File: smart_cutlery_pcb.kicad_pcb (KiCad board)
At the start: 2 copper layers, 55 parts, among them J1 CONN_01X05, J2 CONN_01X04, Q1 Q_PMOS_DGS, Q2 BC849, Q3 BC849, SW1 SW_Push, SW2 SW_Push, U1 STM32L053C6Tx, U2 MODULE-BLUETOOTH-HC-05(34P-27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, U3 NCP1402SN33T1G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

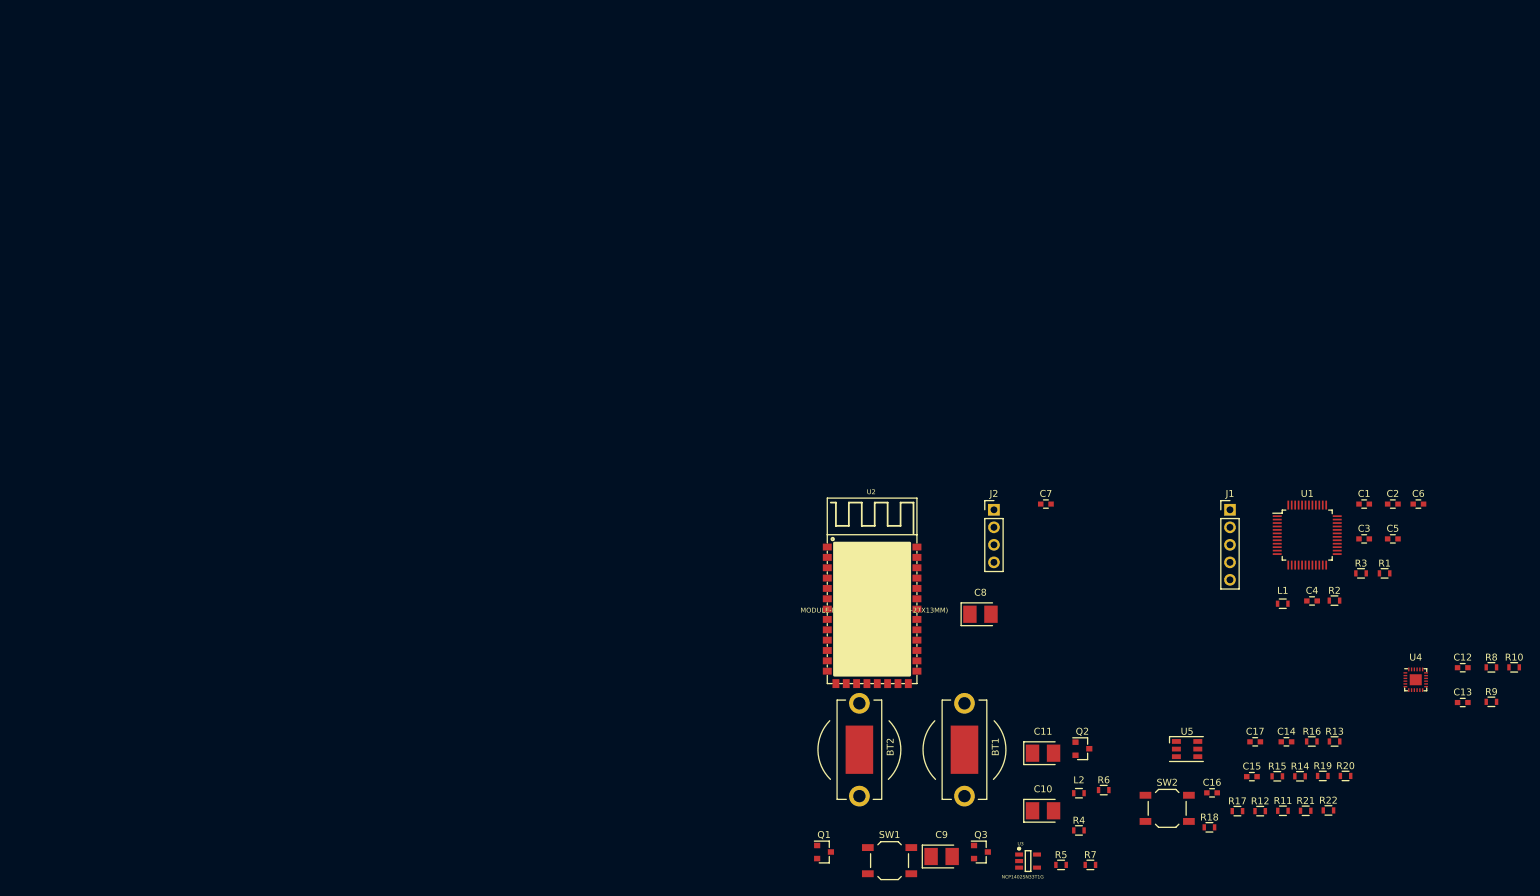
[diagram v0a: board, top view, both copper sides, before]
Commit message: Update to new soft-latching power circuit
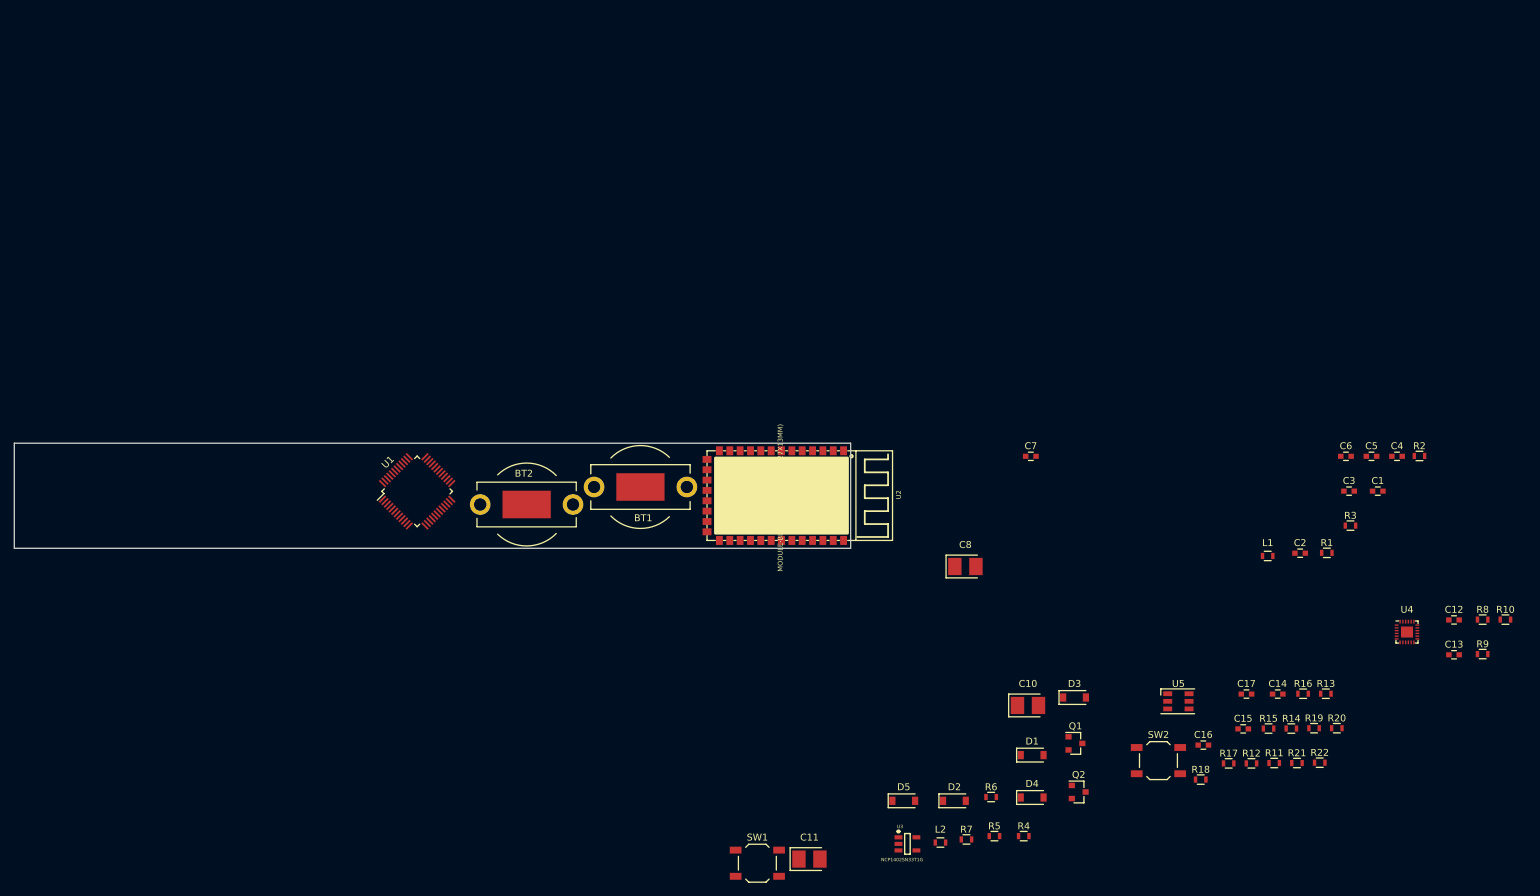
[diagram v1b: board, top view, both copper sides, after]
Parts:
- removed C9: 22uF, Capacitors_Tantalum_SMD:CP_Tantalum_Case-B_EIA-3528-21_Reflow
- removed Q3: BC849, TO_SOT_Packages_SMD:SOT-23
- added D1: MBR0520, Diodes_SMD:D_SOD-123, F.Cu at (210.5, 140.5)
- added D2: MBR0520, Diodes_SMD:D_SOD-123, F.Cu at (199.2, 147.1)
- added D3: MBR0520, Diodes_SMD:D_SOD-123, F.Cu at (216.6, 132.1)
- added D4: MBR0520, Diodes_SMD:D_SOD-123, F.Cu at (210.5, 146.6)
- added D5: MBR0520, Diodes_SMD:D_SOD-123, F.Cu at (191.9, 147.1)
- Q1: value Q_PMOS_DGS -> BSS84
- Q2: value BC849 -> BSS138
- R6: value 1M -> 4K7
- R7: value 100K -> 47K
- SW1, SW2: value SW_Push -> TL3342
- moved U1 129.2 mm to (121.3, 102.2), turned to 45 degrees
- moved BT1 60.5 mm to (153.7, 101.6), turned to 0 degrees
- moved J1 60.2 mm to (179.1, 101.0), turned to 270 degrees
- moved BT2 59.9 mm to (137.2, 104.1), turned to 180 degrees
- moved Q1 39.7 mm to (216.7, 138.8)
- moved C11 37.2 mm to (178.2, 155.6)
- moved U2 36.3 mm to (163.3, 102.8), turned to 270 degrees
- moved J2 34.8 mm to (170.2, 106.0), turned to 90 degrees
- moved R2 24.3 mm to (266.6, 97.1)
- moved C4 24.3 mm to (263.4, 97.2)
- moved L2 21.3 mm to (197.2, 153.2)
- moved SW1 19.2 mm to (170.6, 156.2)
- moved R7 18.3 mm to (200.9, 152.7)
- moved U3 17.7 mm to (192.4, 153.4)
- moved R6 16.4 mm to (204.5, 146.6)
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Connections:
- net /mode_switch renamed /MODE_BTN
- Q1 pad 1: Net-(C10-Pad1) -> Net-(Q1-Pad1)
- Q1 pad 2: Net-(Q1-Pad2) -> Net-(D1-Pad1)
- Q1 pad 3: Net-(D1-Pad1) -> Net-(C10-Pad1)
- Q2 pad 1: Net-(Q2-Pad1) -> /PWR_LATCH
- Q2 pad 3: Net-(Q1-Pad2) -> Net-(Q1-Pad1)
- R11 pad 1: /touch_interface/sense_y1 -> (no net)
- R12 pad 1: /touch_interface/sense_y2 -> (no net)
- R13 pad 1: /touch_interface/sense_y3 -> (no net)
- R14 pad 1: /touch_interface/sense_y4 -> (no net)
- R15 pad 1: /touch_interface/sense_x1 -> (no net)
- R16 pad 1: /touch_interface/sense_x2 -> (no net)
- R17 pad 1: /touch_interface/sense_x3 -> (no net)
- R18 pad 1: /touch_interface/sense_x4 -> (no net)
- R4 pad 1: Net-(D1-Pad1) -> Net-(Q1-Pad1)
- R4 pad 2: Net-(Q1-Pad2) -> Net-(D1-Pad1)
- R5 pad 1: Net-(C10-Pad1) -> GND
- R5 pad 2: Net-(Q2-Pad1) -> /PWR_LATCH
- R6 pad 1: Net-(C10-Pad1) -> /PWR_BUTTON
- R7 pad 1: Net-(D1-Pad1) -> GND
- R7 pad 2: Net-(Q3-Pad3) -> /PWR_BUTTON
- SW1 pad 1: Net-(Q2-Pad1) -> Net-(D1-Pad1)
- SW1 pad 2: Net-(Q3-Pad3) -> Net-(D4-Pad2)
- U1 pad 2: Net-(U1-Pad2) -> (no net)
- U1 pad 20: /micro/PB2 -> (no net)
- U1 pad 25: /micro/PB12 -> (no net)
- U1 pad 27: /micro/PB14 -> /PWR_BUTTON
- U1 pad 28: /micro/PB15 -> /PWR_LATCH
- U1 pad 29: /micro/PA8 -> (no net)
- U1 pad 3: Net-(U1-Pad3) -> (no net)
- U1 pad 33: /micro/PA12 -> (no net)
- U1 pad 38: /micro/PA15 -> (no net)
- U1 pad 4: Net-(U1-Pad4) -> (no net)
- U1 pad 40: /micro/PB4 -> (no net)
- U1 pad 41: /micro/PB5 -> (no net)
- U1 pad 5: Net-(U1-Pad5) -> (no net)
- U1 pad 6: Net-(U1-Pad6) -> (no net)
- U2 pad 10: Net-(U2-Pad10) -> (no net)
- U2 pad 11: Net-(U2-Pad11) -> (no net)
- U2 pad 14: Net-(U2-Pad14) -> (no net)
- U2 pad 15: Net-(U2-Pad15) -> (no net)
- U2 pad 20: Net-(U2-Pad20) -> (no net)
- U2 pad 21: Net-(U2-Pad21) -> (no net)
- U2 pad 22: Net-(U2-Pad22) -> (no net)
- U2 pad 23: Net-(U2-Pad23) -> (no net)
- U2 pad 24: Net-(U2-Pad24) -> (no net)
- U2 pad 25: Net-(U2-Pad25) -> (no net)
- U2 pad 26: Net-(U2-Pad26) -> (no net)
- U2 pad 27: Net-(U2-Pad27) -> (no net)
- U2 pad 28: Net-(U2-Pad28) -> (no net)
- U2 pad 29: Net-(U2-Pad29) -> (no net)
- U2 pad 3: Net-(U2-Pad3) -> (no net)
- U2 pad 30: Net-(U2-Pad30) -> (no net)
- U2 pad 31: Net-(U2-Pad31) -> (no net)
- U2 pad 32: Net-(U2-Pad32) -> (no net)
- U2 pad 33: Net-(U2-Pad33) -> (no net)
- U2 pad 34: Net-(U2-Pad34) -> (no net)
- U2 pad 4: Net-(U2-Pad4) -> (no net)
- U2 pad 5: Net-(U2-Pad5) -> (no net)
- U2 pad 6: Net-(U2-Pad6) -> (no net)
- U2 pad 7: Net-(U2-Pad7) -> (no net)
- U2 pad 8: Net-(U2-Pad8) -> (no net)
- U2 pad 9: Net-(U2-Pad9) -> (no net)
- U4 pad 11: Net-(U4-Pad11) -> (no net)
- U4 pad 12: Net-(U4-Pad12) -> (no net)
- U4 pad 6: Net-(U4-Pad6) -> (no net)
- U4 pad 7: Net-(U4-Pad7) -> (no net)
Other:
- board outline added: 121.3 x 15.2 mm

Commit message: Attempt layout
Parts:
- moved U4 151.9 mm to (115.1, 97.3), turned to 270 degrees
- moved R20 148.9 mm to (110.2, 100.3)
- moved R19 148.4 mm to (107.4, 100.3)
- moved R21 143.8 mm to (112.3, 96.8), turned to 270 degrees
- moved U5 128.0 mm to (108.7, 97.3), turned to 180 degrees
- moved SW2 124.8 mm to (109.2, 105.7), turned to 270 degrees
- moved R2 103.7 mm to (163.3, 106.2)
- moved D3 99.9 mm to (123.2, 96.8)
- moved R3 93.3 mm to (163.3, 107.7)
- moved C10 89.0 mm to (128.5, 97.3), turned to 180 degrees
- moved R6 87.6 mm to (132.8, 96.3)
- moved R7 87.5 mm to (132.8, 97.8), turned to 180 degrees
- moved Q2 87.4 mm to (143.8, 98.6)
- moved L2 85.7 mm to (130.0, 99.8), turned to 180 degrees
- moved R5 85.3 mm to (140.5, 96.5)
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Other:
- board size 121.3 x 15.2 mm -> 127.4 x 15.5 mm

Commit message: attempt 1
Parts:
- removed BT2: 3V CR1225, BC_2011_CR1225_HOLDER:BC-2011-CR1225
- removed C17: 100nF, Capacitors_SMD:C_0603
- removed D2: MBR0520, Diodes_SMD:D_SOD-123
- removed R22: 10K, Resistors_SMD:R_0603
- removed SW2: TL3342, Buttons_Switches_SMD:SW_SPST_TL3342
- U4: moved to B.Cu
- moved R10 147.7 mm to (142.2, 65.2), turned to 180 degrees
- moved R8 146.2 mm to (140.2, 66.0), turned to 90 degrees
- moved R9 143.8 mm to (144.8, 66.8)
- moved C12 126.6 mm to (152.8, 77.5), turned to 90 degrees
- moved C13 126.1 mm to (159.2, 68.8), turned to 90 degrees
- moved C4 125.2 mm to (140.2, 74.8), turned to 90 degrees
- moved C1 124.8 mm to (140.2, 69.0), turned to 90 degrees
- moved R11 124.3 mm to (147.8, 65.0)
- moved C5 121.2 mm to (142.0, 68.0), turned to 90 degrees
- moved C3 120.0 mm to (140.2, 72.0), turned to 90 degrees
- moved R12 118.5 mm to (150.5, 66.8)
- moved R1 117.6 mm to (145.0, 65.0)
- moved R18 115.6 mm to (150.5, 65.0), turned to 180 degrees
- moved R13 114.7 mm to (153.2, 75.0)
- moved R17 113.7 mm to (153.5, 66.8)
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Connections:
- R11 pad 1: (no net) -> /touch_interface/sense_y1
- R12 pad 1: (no net) -> /touch_interface/sense_y2
- R13 pad 1: (no net) -> /touch_interface/sense_y3
- R14 pad 1: (no net) -> /touch_interface/sense_y4
- R15 pad 1: (no net) -> /touch_interface/sense_x1
- R16 pad 1: (no net) -> /touch_interface/sense_x2
- R17 pad 1: (no net) -> /touch_interface/sense_x3
- R18 pad 1: (no net) -> /touch_interface/sense_x4
- U1 pad 2: (no net) -> Net-(U1-Pad2)
- U1 pad 20: (no net) -> /micro/PB2
- U1 pad 25: (no net) -> /micro/PB12
- U1 pad 26: /MODE_BTN -> /micro/PB13
- U1 pad 29: (no net) -> /micro/PA8
- U1 pad 3: (no net) -> Net-(U1-Pad3)
- U1 pad 33: (no net) -> /micro/PA12
- U1 pad 38: (no net) -> /micro/PA15
- U1 pad 4: (no net) -> Net-(U1-Pad4)
- U1 pad 40: (no net) -> /micro/PB4
- U1 pad 41: (no net) -> /micro/PB5
- U1 pad 5: (no net) -> Net-(U1-Pad5)
- U1 pad 6: (no net) -> Net-(U1-Pad6)
- U2 pad 10: (no net) -> Net-(U2-Pad10)
- U2 pad 11: (no net) -> Net-(U2-Pad11)
- U2 pad 14: (no net) -> Net-(U2-Pad14)
- U2 pad 15: (no net) -> Net-(U2-Pad15)
- U2 pad 20: (no net) -> Net-(U2-Pad20)
- U2 pad 21: (no net) -> Net-(U2-Pad21)
- U2 pad 22: (no net) -> Net-(U2-Pad22)
- U2 pad 23: (no net) -> Net-(U2-Pad23)
- U2 pad 24: (no net) -> Net-(U2-Pad24)
- U2 pad 25: (no net) -> Net-(U2-Pad25)
- U2 pad 26: (no net) -> Net-(U2-Pad26)
- U2 pad 27: (no net) -> Net-(U2-Pad27)
- U2 pad 28: (no net) -> Net-(U2-Pad28)
- U2 pad 29: (no net) -> Net-(U2-Pad29)
- U2 pad 3: (no net) -> Net-(U2-Pad3)
- U2 pad 30: (no net) -> Net-(U2-Pad30)
- U2 pad 31: (no net) -> Net-(U2-Pad31)
- U2 pad 32: (no net) -> Net-(U2-Pad32)
- U2 pad 33: (no net) -> Net-(U2-Pad33)
- U2 pad 34: (no net) -> Net-(U2-Pad34)
- U2 pad 4: (no net) -> Net-(U2-Pad4)
- U2 pad 5: (no net) -> Net-(U2-Pad5)
- U2 pad 6: (no net) -> Net-(U2-Pad6)
- U2 pad 7: (no net) -> Net-(U2-Pad7)
- U2 pad 8: (no net) -> Net-(U2-Pad8)
- U2 pad 9: (no net) -> Net-(U2-Pad9)
- U4 pad 11: (no net) -> Net-(U4-Pad11)
- U4 pad 12: (no net) -> Net-(U4-Pad12)
- U4 pad 6: (no net) -> Net-(U4-Pad6)
- U4 pad 7: (no net) -> Net-(U4-Pad7)
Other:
- board size 127.4 x 15.5 mm -> 95 x 19.5 mm

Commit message: More changes, replace
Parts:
- removed C4, C6: 1uF, Capacitors_SMD:C_0603
- removed D1: MBR0520, Diodes_SMD:D_SOD-123
- J1, J2, R2, R3: moved to B.Cu
- moved R10 41.7 mm to (176.0, 40.8), turned to 270 degrees
- moved R8 39.4 mm to (170.5, 40.8)
- moved C12 39.3 mm to (166.8, 40.8)
- moved R9 38.2 mm to (172.8, 40.8), turned to 270 degrees
- moved U4 36.6 mm to (171.2, 34.8)
- moved C13 29.5 mm to (168.5, 40.8)
- moved C3 21.1 mm to (161.2, 74.7), turned to 0 degrees
- moved C1 20.1 mm to (160.2, 66.4), turned to 270 degrees
- moved R1 17.1 mm to (160.3, 72.6), turned to 270 degrees
- moved C5 14.7 mm to (156.2, 64.3), turned to 180 degrees
- moved R19 14.6 mm to (147.5, 69.8), turned to 0 degrees
- moved Q2 14.4 mm to (177.8, 64.8), turned to 270 degrees
- moved R16 14.1 mm to (142.3, 65.6), turned to 270 degrees
- moved R15 13.3 mm to (145.4, 65.5), turned to 270 degrees
- moved R13 13.1 mm to (140.8, 71.0), turned to 90 degrees
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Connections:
- Q1 pad 2: Net-(D1-Pad1) -> /BAT1_VSENSE
- R4 pad 2: Net-(D1-Pad1) -> /BAT1_VSENSE
- SW1 pad 1: Net-(D1-Pad1) -> /BAT1_VSENSE

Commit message: Do some routing
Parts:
- C12, C13, R10, R8, R9: moved to B.Cu
- moved U4 34.9 mm to (168.5, 69.5)
- moved R8 31.6 mm to (168.7, 72.3), turned to 180 degrees
- moved C13 29.6 mm to (171.2, 70.2)
- moved C12 28.6 mm to (165.8, 69.3), turned to 270 degrees
- moved R10 27.7 mm to (166.4, 66.7), turned to 180 degrees
- moved R9 26.2 mm to (169.0, 66.7), turned to 180 degrees
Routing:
- net Net-(D4-Pad2): track 0.00 -> 67.0 mm, vias 0 -> 4
- net +3V3: track 0.00 -> 59.7 mm, vias 0 -> 4
- net Net-(C10-Pad1): track 0.00 -> 53.7 mm, vias 0 -> 3
- net /BAT1_VSENSE: track 0.00 -> 53.0 mm, vias 0 -> 5
- net Net-(J2-Pad4): track 0.00 -> 15.9 mm
- net /PWR_LATCH: track 0.00 -> 15.5 mm
- net /touch_y2: track 0.00 -> 12.8 mm, vias 0 -> 2
- net Net-(J2-Pad3): track 0.00 -> 12.6 mm
- net Net-(R21-Pad1): track 0.00 -> 11.9 mm, vias 0 -> 2
- net GND: track 0.00 -> 11.2 mm, vias 0 -> 18
- net /LED_RED: track 0.00 -> 10.8 mm, vias 0 -> 2
- net Net-(Q1-Pad1): track 0.00 -> 10.5 mm
- net Net-(C5-Pad1): track 0.00 -> 10.4 mm, vias 0 -> 2
- net Net-(J2-Pad2): track 0.00 -> 9.51 mm
- net Net-(D3-Pad2): track 0.00 -> 9.31 mm, vias 0 -> 2
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- added copper zone on B.Cu, net GND
- added copper zone on F.Cu, net GND

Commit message: More routing
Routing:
- net /BLUETOOTH_TX: track 0.00 -> 56.6 mm, vias 0 -> 2
- net /BLUETOOTH_RX: track 0.00 -> 53.9 mm, vias 0 -> 2
- net /micro/nRST: track 0.00 -> 37.2 mm, vias 0 -> 1
- net /micro/SWD_IO: track 0.00 -> 34.4 mm, vias 0 -> 3
- net /micro/SWD_CLK: track 0.00 -> 32.6 mm, vias 0 -> 1
- net /PWR_LATCH: track 15.5 -> 46.2 mm, vias 0 -> 4
- net /PWR_BUTTON: track 2.00 -> 29.4 mm, vias 0 -> 2
- net +3V3: track 59.7 -> 86.1 mm, vias 4 -> 6
- net GND: track 11.2 -> 17.0 mm, vias 18 -> 19

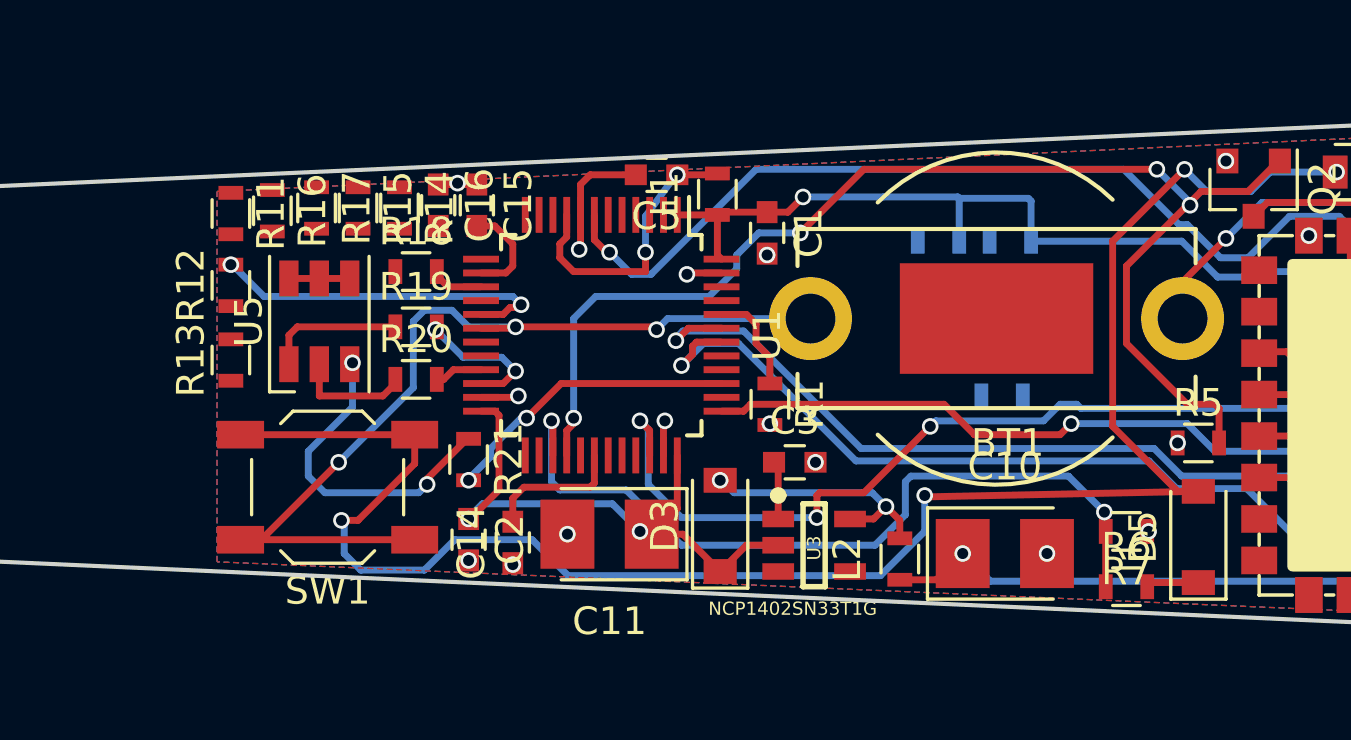
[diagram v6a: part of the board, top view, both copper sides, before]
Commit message: finish basic routing
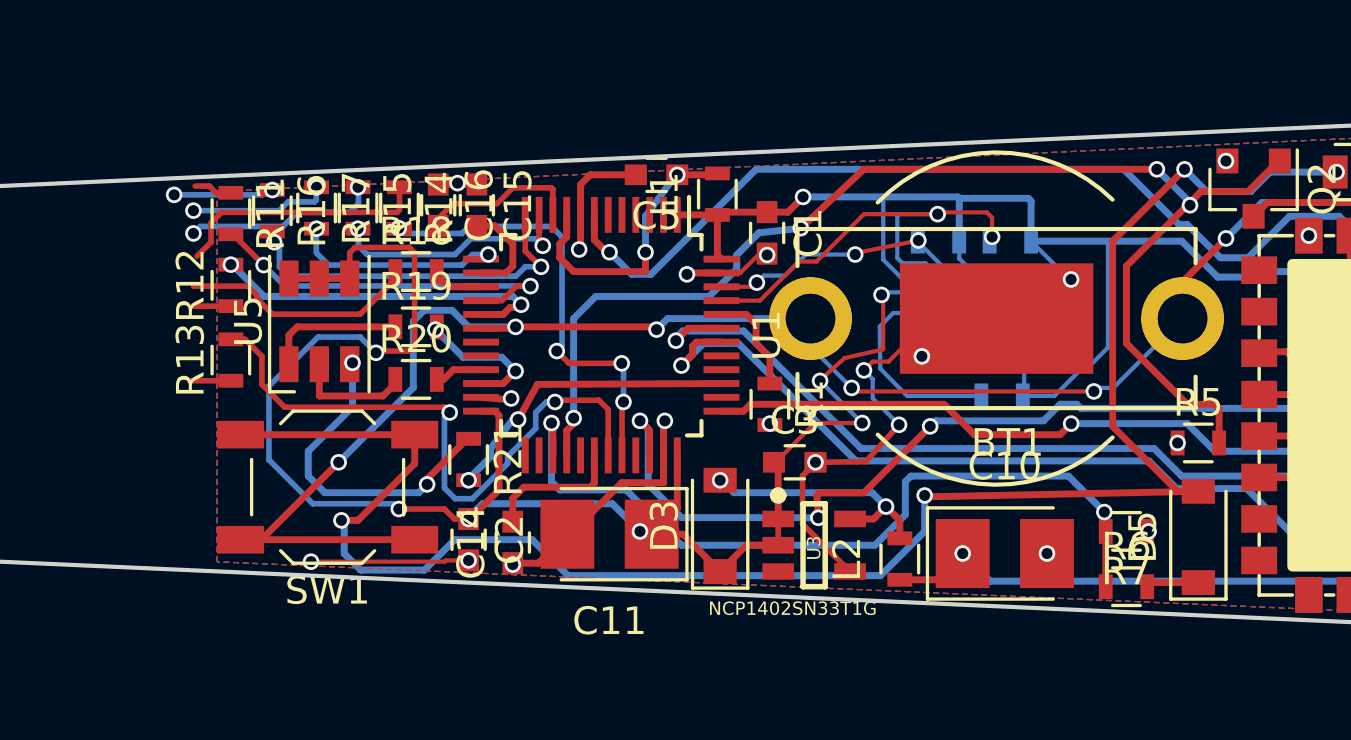
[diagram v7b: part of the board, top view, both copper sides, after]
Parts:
- moved C13 1.18 mm to (171.2, 69.0)
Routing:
- net +3V3: track 86.1 -> 140.7 mm, vias 6 -> 11
- net GND: track 17.0 -> 59.0 mm, vias 19 -> 23
- net /touch_y3: track 0.00 -> 22.3 mm, vias 0 -> 2
- net /ACCEL_GYRO_I2C_SCL: track 0.00 -> 18.3 mm, vias 0 -> 2
- net /touch_y4: track 0.00 -> 16.4 mm, vias 0 -> 4
- net /BAT1_VSENSE: track 53.0 -> 69.3 mm, vias 5 -> 7
- net /touch_y1: track 0.00 -> 13.6 mm, vias 0 -> 2
- net /touch_x2: track 0.00 -> 13.2 mm, vias 0 -> 2
- net /ACCEL_GYRO_I2C_SDA: track 0.00 -> 10.1 mm, vias 0 -> 3
- net /touch_interface/sense_y4: track 0.00 -> 9.25 mm
- net /touch_x1: track 0.00 -> 8.96 mm, vias 0 -> 2
- net /touch_interface/sense_x4: track 0.00 -> 8.60 mm
- net Net-(R8-Pad2): track 0.00 -> 8.52 mm
- net /touch_x3: track 0.00 -> 7.77 mm, vias 0 -> 2
- net /touch_interface/sense_x1: track 0.00 -> 7.19 mm, vias 0 -> 2
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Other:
- net class Default: clearance 0.2 -> 0.152
- rule trace_clearance: 0.2 -> 0.152
- rule trace_min: 0.2 -> 0.152
